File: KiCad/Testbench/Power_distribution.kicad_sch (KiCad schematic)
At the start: 13 parts, among them J18 Conn_02x03_Counter_Clockwise

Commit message: PCB before first processing
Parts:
- renumbered D14 to D17, D15 to D18, D16 to D19, D17 to D20, D18 to D21, D19 to D22, R16 to R19, R17 to R20, R18 to R21, R19 to R22, R20 to R23, R21 to R24
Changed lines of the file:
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@@
 		(dnp no)
 		(fields_autoplaced yes)
-		(property "Reference" "D14"
+		(property "Reference" "D17"
 			(at 40.64 165.4174 90)
 			(effects
@@
 			(project "Testbench"
 				(path "/7bff671f-2f7d-4dcb-82cb-7f168fb2ab46/9c030398-53e0-40c8-9b81-060e50b2ba02"
-					(reference "D14")
+					(reference "D17")
 					(unit 1)
 				)
@@
 		(dnp no)
 		(fields_autoplaced yes)
-		(property "Reference" "R21"
+		(property "Reference" "R24"
 			(at 224.79 59.6899 0)
 			(effects
@@
 			(project "Testbench"
 				(path "/7bff671f-2f7d-4dcb-82cb-7f168fb2ab46/9c030398-53e0-40c8-9b81-060e50b2ba02"
-					(reference "R21")
+					(reference "R24")
 					(unit 1)
 				)
@@
 		(on_board yes)
 		(dnp no)
-		(property "Reference" "#PWR018"
+		(property "Reference" "#PWR021"
 			(at 36.83 182.88 0)
 			(effects
@@
 			(project "Testbench"
 				(path "/7bff671f-2f7d-4dcb-82cb-7f168fb2ab46/9c030398-53e0-40c8-9b81-060e50b2ba02"
-					(reference "#PWR018")
+					(reference "#PWR021")
 					(unit 1)
 				)
@@
 		(dnp no)
 		(fields_autoplaced yes)
-		(property "Reference" "D16"
+		(property "Reference" "D19"
 			(at 102.87 73.9774 90)
 			(effects
@@
 			(project "Testbench"
 				(path "/7bff671f-2f7d-4dcb-82cb-7f168fb2ab46/9c030398-53e0-40c8-9b81-060e50b2ba02"
-					(reference "D16")
+					(reference "D19")
 					(unit 1)
 				)
@@
 		(on_board yes)
 		(dnp no)
-		(property "Reference" "#PWR020"
+		(property "Reference" "#PWR023"
 			(at 99.06 91.44 0)
 			(effects
@@
 			(project "Testbench"
 				(path "/7bff671f-2f7d-4dcb-82cb-7f168fb2ab46/9c030398-53e0-40c8-9b81-060e50b2ba02"
-					(reference "#PWR020")
+					(reference "#PWR023")
 					(unit 1)
 				)
@@
 		(dnp no)
 		(fields_autoplaced yes)
-		(property "Reference" "R20"
+		(property "Reference" "R23"
 			(at 162.56 59.6899 0)
 			(effects
@@
 			(project "Testbench"
 				(path "/7bff671f-2f7d-4dcb-82cb-7f168fb2ab46/9c030398-53e0-40c8-9b81-060e50b2ba02"
-					(reference "R20")
+					(reference "R23")
 					(unit 1)
 				)
@@
 		(dnp no)
 		(fields_autoplaced yes)
-		(property "Reference" "R16"
+		(property "Reference" "R19"
 			(at 39.37 151.1299 0)
 			(effects
@@
 			(project "Testbench"
 				(path "/7bff671f-2f7d-4dcb-82cb-7f168fb2ab46/9c030398-53e0-40c8-9b81-060e50b2ba02"
-					(reference "R16")
+					(reference "R19")
 					(unit 1)
 				)
@@
 		(dnp no)
 		(fields_autoplaced yes)
-		(property "Reference" "D17"
+		(property "Reference" "D20"
 			(at 102.87 165.4174 90)
 			(effects
@@
 			(project "Testbench"
 				(path "/7bff671f-2f7d-4dcb-82cb-7f168fb2ab46/9c030398-53e0-40c8-9b81-060e50b2ba02"
-					(reference "D17")
+					(reference "D20")
 					(unit 1)
 				)
@@
 		(on_board yes)
 		(dnp no)
-		(property "Reference" "#PWR023"
+		(property "Reference" "#PWR026"
 			(at 222.25 91.44 0)
 			(effects
@@
 			(project "Testbench"
 				(path "/7bff671f-2f7d-4dcb-82cb-7f168fb2ab46/9c030398-53e0-40c8-9b81-060e50b2ba02"
-					(reference "#PWR023")
+					(reference "#PWR026")
 					(unit 1)
 				)
@@
 		(on_board yes)
 		(dnp no)
-		(property "Reference" "#PWR021"
+		(property "Reference" "#PWR024"
 			(at 99.06 182.88 0)
 			(effects
@@
 			(project "Testbench"
 				(path "/7bff671f-2f7d-4dcb-82cb-7f168fb2ab46/9c030398-53e0-40c8-9b81-060e50b2ba02"
-					(reference "#PWR021")
+					(reference "#PWR024")
 					(unit 1)
 				)
@@
 		(dnp no)
 		(fields_autoplaced yes)
-		(property "Reference" "D15"
+		(property "Reference" "D18"
 			(at 41.91 73.9774 90)
 			(effects
@@
 			(project "Testbench"
 				(path "/7bff671f-2f7d-4dcb-82cb-7f168fb2ab46/9c030398-53e0-40c8-9b81-060e50b2ba02"
-					(reference "D15")
+					(reference "D18")
 					(unit 1)
 				)
@@
 		(on_board yes)
 		(dnp no)
-		(property "Reference" "#PWR019"
+		(property "Reference" "#PWR022"
 			(at 38.1 91.44 0)
 			(effects
@@
 			(project "Testbench"
 				(path "/7bff671f-2f7d-4dcb-82cb-7f168fb2ab46/9c030398-53e0-40c8-9b81-060e50b2ba02"
-					(reference "#PWR019")
+					(reference "#PWR022")
 					(unit 1)
 				)
@@
 		(dnp no)
 		(fields_autoplaced yes)
-		(property "Reference" "D19"
+		(property "Reference" "D22"
 			(at 226.06 73.9774 90)
 			(effects
@@
 			(project "Testbench"
 				(path "/7bff671f-2f7d-4dcb-82cb-7f168fb2ab46/9c030398-53e0-40c8-9b81-060e50b2ba02"
-					(reference "D19")
+					(reference "D22")
 					(unit 1)
 				)
@@
 		(dnp no)
 		(fields_autoplaced yes)
-		(property "Reference" "R18"
+		(property "Reference" "R21"
 			(at 101.6 59.6899 0)
 			(effects
@@
 			(project "Testbench"
 				(path "/7bff671f-2f7d-4dcb-82cb-7f168fb2ab46/9c030398-53e0-40c8-9b81-060e50b2ba02"
-					(reference "R18")
+					(reference "R21")
 					(unit 1)
 				)
@@
 		(dnp no)
 		(fields_autoplaced yes)
-		(property "Reference" "R19"
+		(property "Reference" "R22"
 			(at 101.6 151.1299 0)
 			(effects
@@
 			(project "Testbench"
 				(path "/7bff671f-2f7d-4dcb-82cb-7f168fb2ab46/9c030398-53e0-40c8-9b81-060e50b2ba02"
-					(reference "R19")
+					(reference "R22")
 					(unit 1)
 				)
@@
 		(dnp no)
 		(fields_autoplaced yes)
-		(property "Reference" "D18"
+		(property "Reference" "D21"
 			(at 163.83 73.9774 90)
 			(effects
@@
 			(project "Testbench"
 				(path "/7bff671f-2f7d-4dcb-82cb-7f168fb2ab46/9c030398-53e0-40c8-9b81-060e50b2ba02"
-					(reference "D18")
+					(reference "D21")
 					(unit 1)
 				)
@@
 		(dnp no)
 		(fields_autoplaced yes)
-		(property "Reference" "R17"
+		(property "Reference" "R20"
 			(at 40.64 59.6899 0)
 			(effects
@@
 			(project "Testbench"
 				(path "/7bff671f-2f7d-4dcb-82cb-7f168fb2ab46/9c030398-53e0-40c8-9b81-060e50b2ba02"
-					(reference "R17")
+					(reference "R20")
 					(unit 1)
 				)
@@
 		(on_board yes)
 		(dnp no)
-		(property "Reference" "#PWR022"
+		(property "Reference" "#PWR025"
 			(at 160.02 91.44 0)
 			(effects
@@
 			(project "Testbench"
 				(path "/7bff671f-2f7d-4dcb-82cb-7f168fb2ab46/9c030398-53e0-40c8-9b81-060e50b2ba02"
-					(reference "#PWR022")
-					(unit 1)
-				)
+					(reference "#PWR025")
+					(unit 1)
+				)

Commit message: After work 151024
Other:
- moved on the sheet: J18
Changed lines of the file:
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@@
 	(wire
 		(pts
-			(xy 190.5 143.51) (xy 198.12 143.51)
+			(xy 171.45 130.81) (xy 179.07 130.81)
 		)
 		(stroke
@@
 	(wire
 		(pts
-			(xy 210.82 146.05) (xy 213.36 146.05)
+			(xy 191.77 133.35) (xy 194.31 133.35)
 		)
 		(stroke
@@
 	(wire
 		(pts
-			(xy 190.5 140.97) (xy 198.12 140.97)
-		)
-		(stroke
-			(width 0)
-			(type default)
-		)
-	)
-	(wire
-		(pts
-			(xy 210.82 143.51) (xy 213.36 143.51)
-		)
-		(stroke
-			(width 0)
-			(type default)
-		)
-	)
-	(wire
-		(pts
-			(xy 190.5 146.05) (xy 198.12 146.05)
+			(xy 171.45 128.27) (xy 179.07 128.27)
+		)
+		(stroke
+			(width 0)
+			(type default)
+		)
+	)
+	(wire
+		(pts
+			(xy 191.77 130.81) (xy 194.31 130.81)
+		)
+		(stroke
+			(width 0)
+			(type default)
+		)
+	)
+	(wire
+		(pts
+			(xy 171.45 133.35) (xy 179.07 133.35)
 		)
 		(stroke
@@
 	(wire
 		(pts
-			(xy 210.82 140.97) (xy 213.36 140.97)
+			(xy 191.77 128.27) (xy 194.31 128.27)
 		)
 		(stroke
@@
 	)
 	(label "2-E1"
-		(at 213.36 140.97 0)
+		(at 194.31 128.27 0)
 		(fields_autoplaced yes)
 		(effects
@@
 	)
 	(label "2-C1"
-		(at 213.36 146.05 0)
+		(at 194.31 133.35 0)
 		(fields_autoplaced yes)
 		(effects
@@
 	)
 	(label "2-B1"
-		(at 213.36 143.51 0)
+		(at 194.31 130.81 0)
 		(fields_autoplaced yes)
 		(effects
@@
 	)
 	(label "2-D1"
-		(at 190.5 146.05 0)
+		(at 171.45 133.35 0)
 		(fields_autoplaced yes)
 		(effects
@@
 	)
 	(label "2-A1"
-		(at 190.5 143.51 0)
+		(at 171.45 130.81 0)
 		(fields_autoplaced yes)
 		(effects
@@
 	)
 	(label "2-A4"
-		(at 190.5 140.97 0)
+		(at 171.45 128.27 0)
 		(fields_autoplaced yes)
 		(effects
@@
 	(symbol
 		(lib_id "Connector_Generic:Conn_02x03_Counter_Clockwise")
-		(at 203.2 143.51 0)
+		(at 184.15 130.81 0)
 		(unit 1)
 		(exclude_from_sim no)
@@
 		(fields_autoplaced yes)
 		(property "Reference" "J18"
-			(at 204.47 134.62 0)
+			(at 185.42 121.92 0)
 			(effects
 				(font
@@
 		)
 		(property "Value" "Conn_02x03_Counter_Clockwise"
-			(at 204.47 137.16 0)
+			(at 185.42 124.46 0)
 			(effects
 				(font
@@
 		)
 		(property "Footprint" "Connector_Molex:Molex_Mini-Fit_Jr_5566-06A_2x03_P4.20mm_Vertical"
-			(at 203.2 143.51 0)
+			(at 184.15 130.81 0)
 			(effects
 				(font
@@
 		)
 		(property "Datasheet" "~"
-			(at 203.2 143.51 0)
+			(at 184.15 130.81 0)
 			(effects
 				(font
@@
 		)
 		(property "Description" "Generic connector, double row, 02x03, counter clockwise pin numbering scheme (similar to DIP package numbering), script generated (kicad-library-utils/schlib/autogen/connector/)"
-			(at 203.2 143.51 0)
-			(effects
-				(font
+			(at 184.15 130.81 0)
+			(effects
+				(font

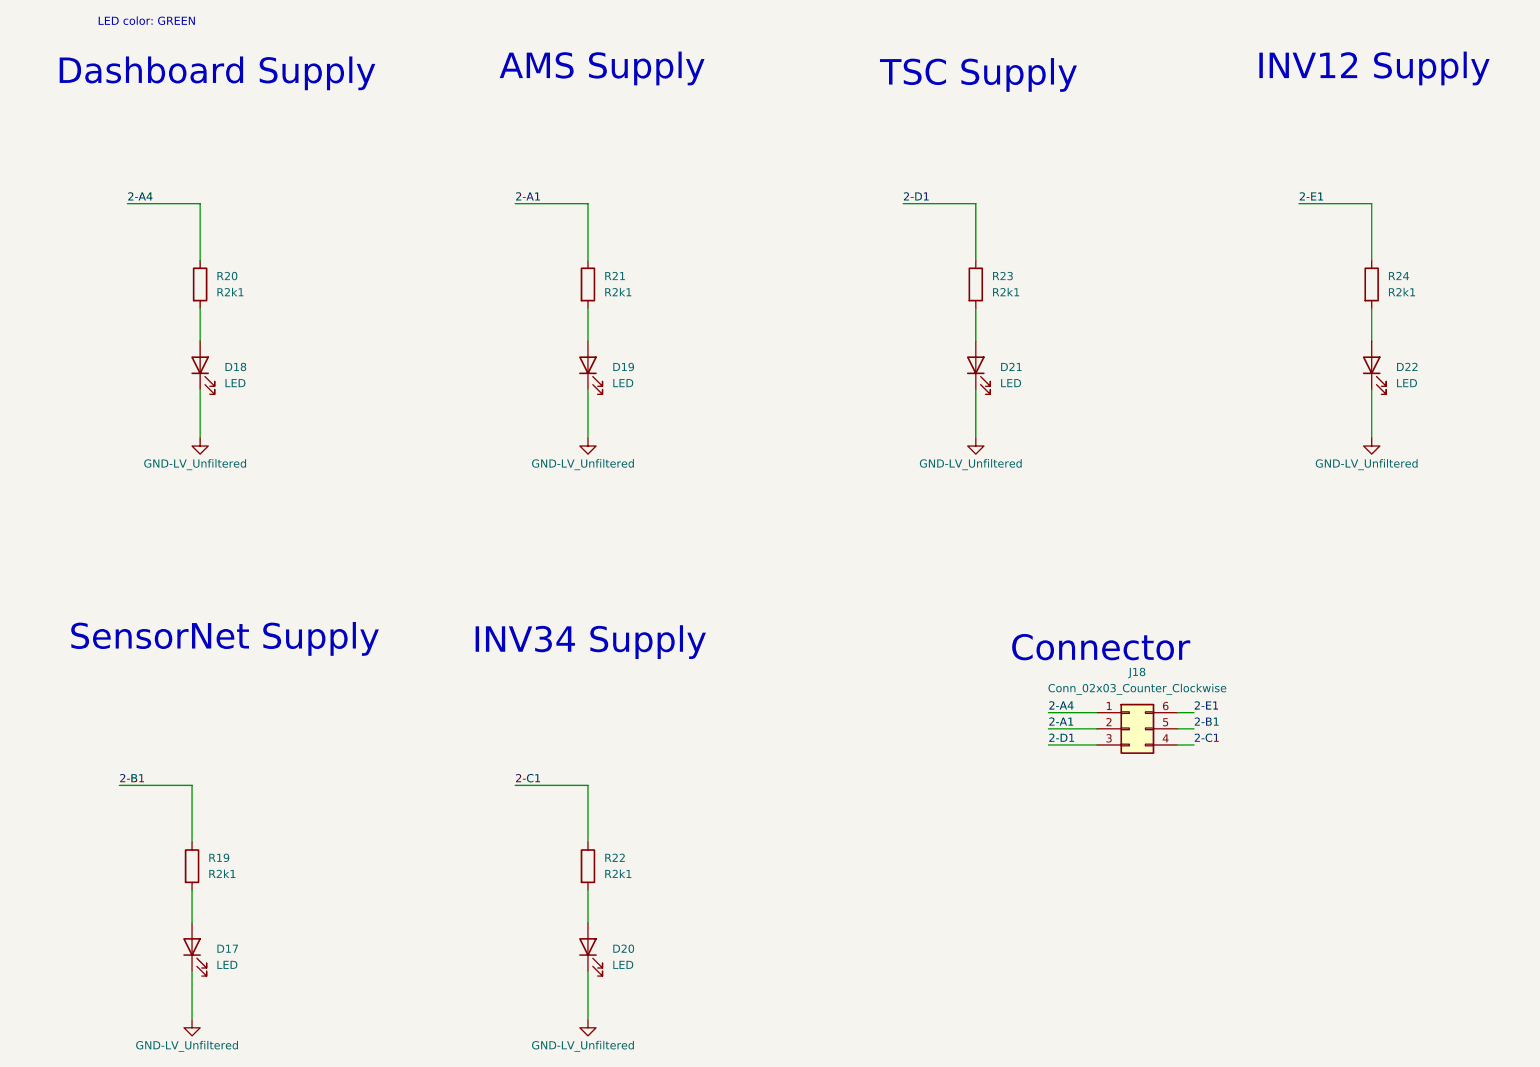
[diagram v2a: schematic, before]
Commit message: Updated for PCBV2 Updated size and added LED.
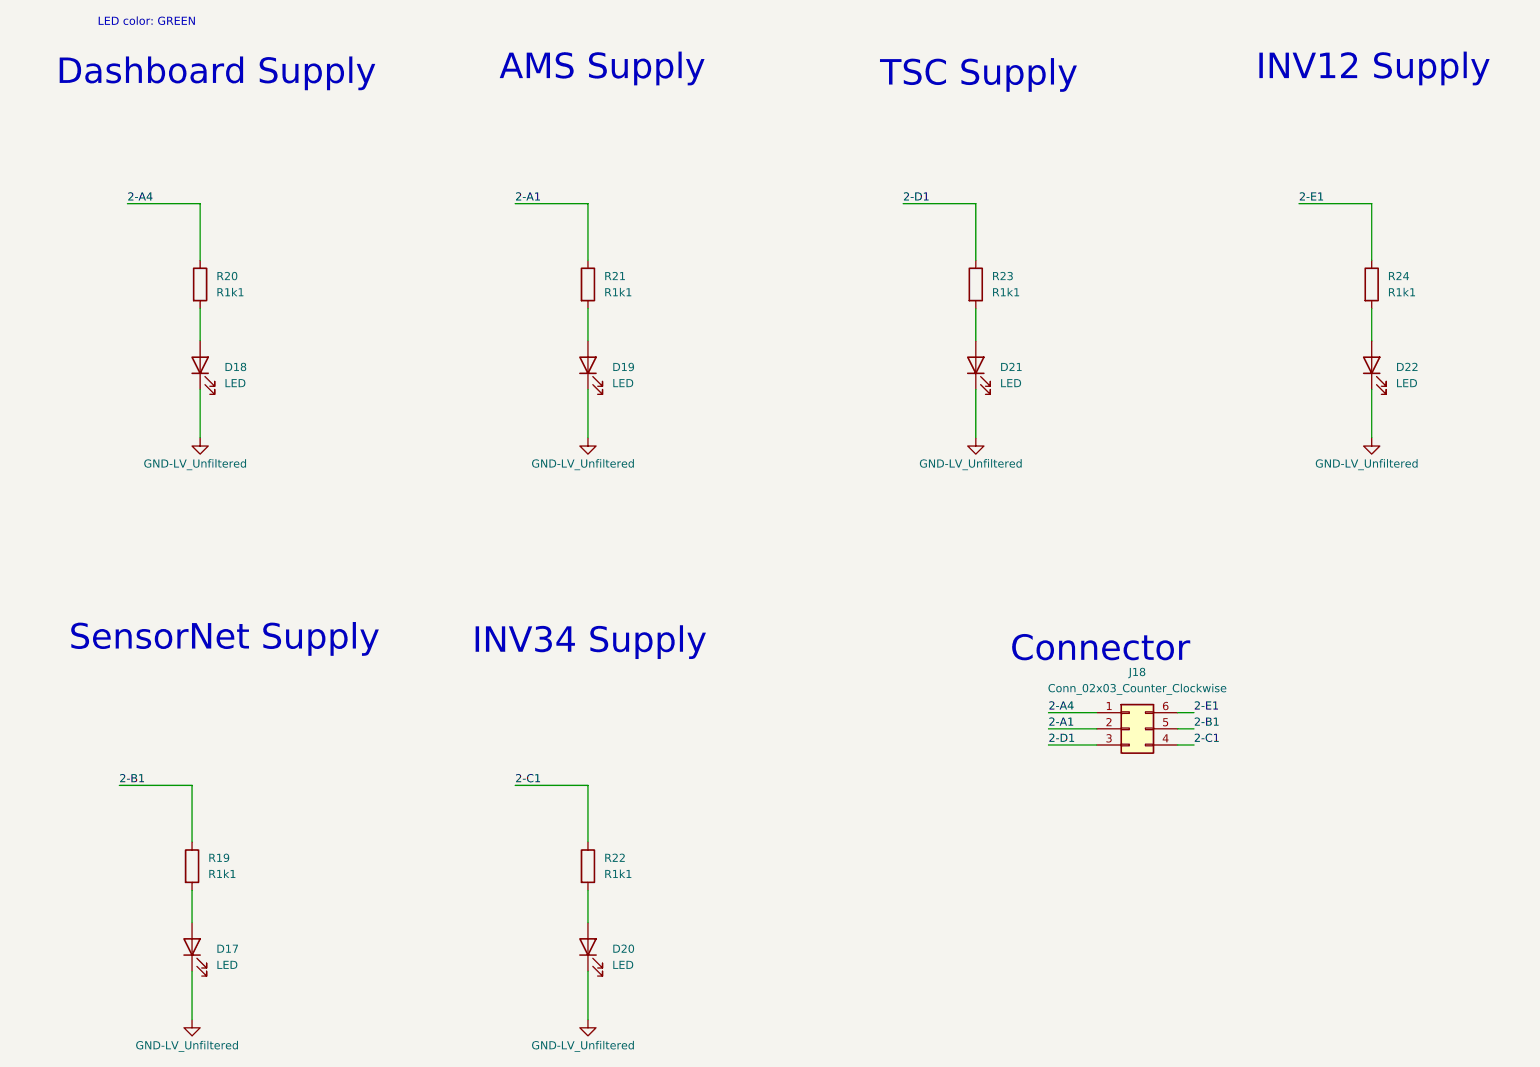
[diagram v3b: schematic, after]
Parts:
- R19, R20, R21, R22, R23, R24: value R2k1 -> R1k1
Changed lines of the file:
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@@
 			)
 		)
-		(property "Value" "R2k1"
+		(property "Value" "R1k1"
 			(at 224.79 62.2299 0)
 			(effects
@@
 			)
 		)
-		(property "Value" "R2k1"
+		(property "Value" "R1k1"
 			(at 162.56 62.2299 0)
 			(effects
@@
 			)
 		)
-		(property "Value" "R2k1"
+		(property "Value" "R1k1"
 			(at 39.37 153.6699 0)
 			(effects
@@
 			)
 		)
-		(property "Value" "R2k1"
+		(property "Value" "R1k1"
 			(at 101.6 62.2299 0)
 			(effects
@@
 			)
 		)
-		(property "Value" "R2k1"
+		(property "Value" "R1k1"
 			(at 101.6 153.6699 0)
 			(effects
@@
 			)
 		)
-		(property "Value" "R2k1"
+		(property "Value" "R1k1"
 			(at 40.64 62.2299 0)
 			(effects
